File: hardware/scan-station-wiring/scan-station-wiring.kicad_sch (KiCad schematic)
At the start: 55 parts, among them J1A CYD Expansion (SPI2), J1B CYD UART (PWR+HS), J2 NFC Antenna A, J3 RGB LED Header, J4 NFC Antenna B, J5 USB-C Power, J6 Load Cell, J7 CAN Bus, J8 I2C1 Expansion, J9 TOF Sensor (I2C1), Q1 TVDD_SW_A, Q2 TVDD_SW_B, Q3 BSS138 (SDA), Q4 BSS138 (SCL), U1 ESP32-S3-DevKitC-1, U2 ADS1220IPWR, U3 AHT20, U4 PN5180A0HN, U5 AS7341-DLGM, U6 AMS1117-3.3, U7 SN65HVD230DR, U8 AMS1117-1.8, Y1 27.12MHz

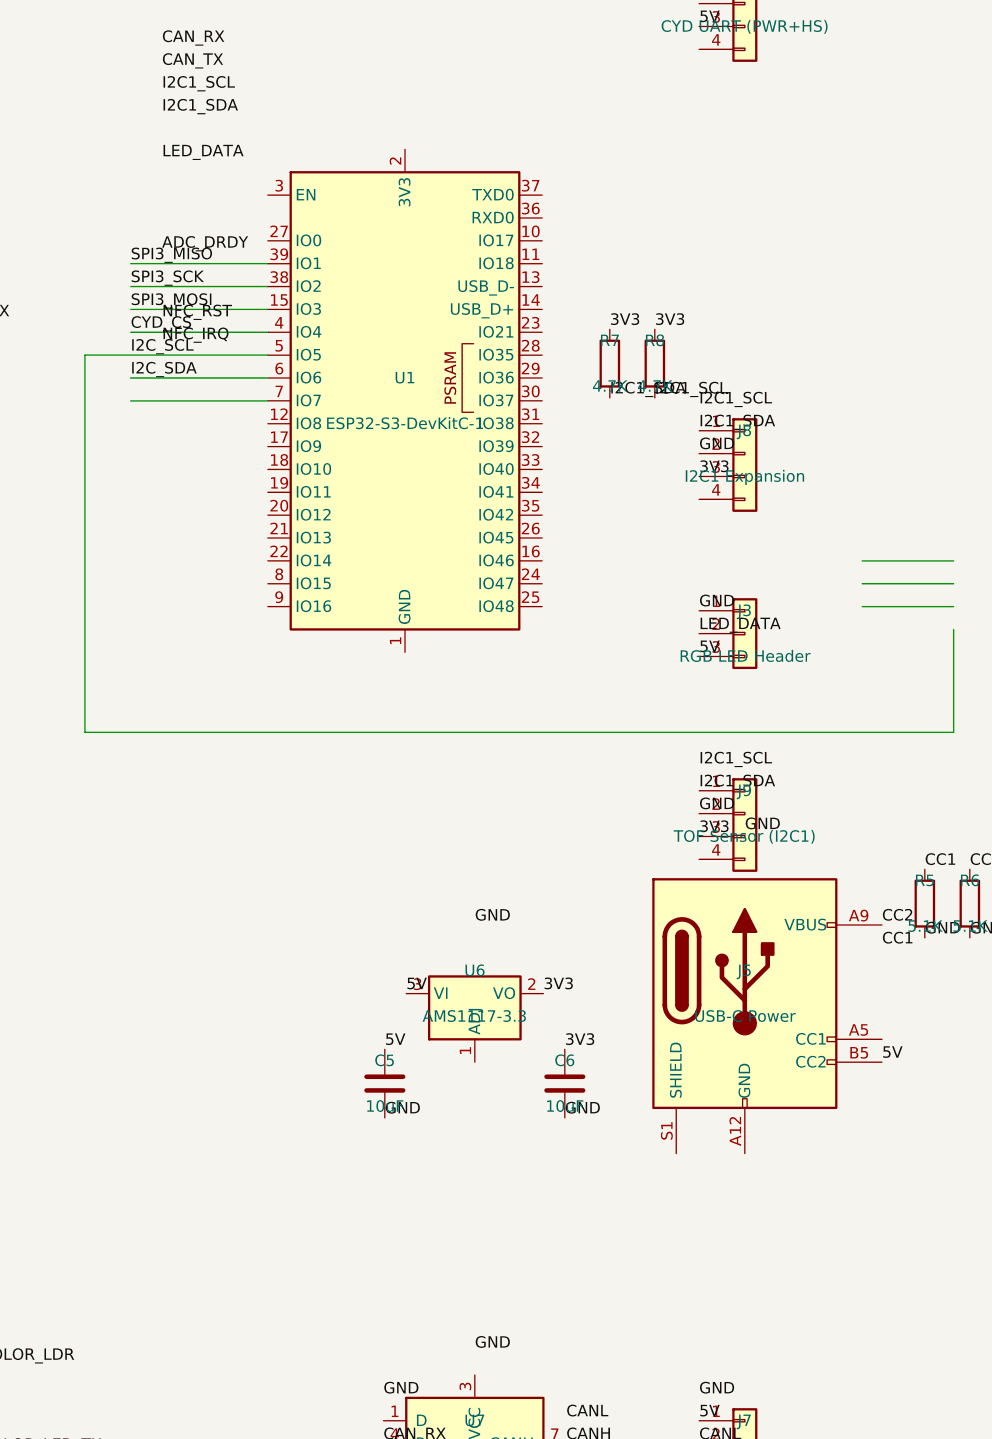
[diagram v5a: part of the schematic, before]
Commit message: feat: add button/encoder header for non-touchscreen operation
J10: 5-pin header for rotary encoder (A/B/SW) or 3 buttons
- BTN_A (IO35), BTN_B (IO36), BTN_SW (IO37) + 3V3 + GND
- Enables non-CYD configurations (SPI OLED + physical controls)
- CYD_SPARE/CYD_READY pins double as DC/RST for dumb SPI displays

Co-Authored-By: Claude Opus 4.6 (1M context) <noreply@anthropic.com>
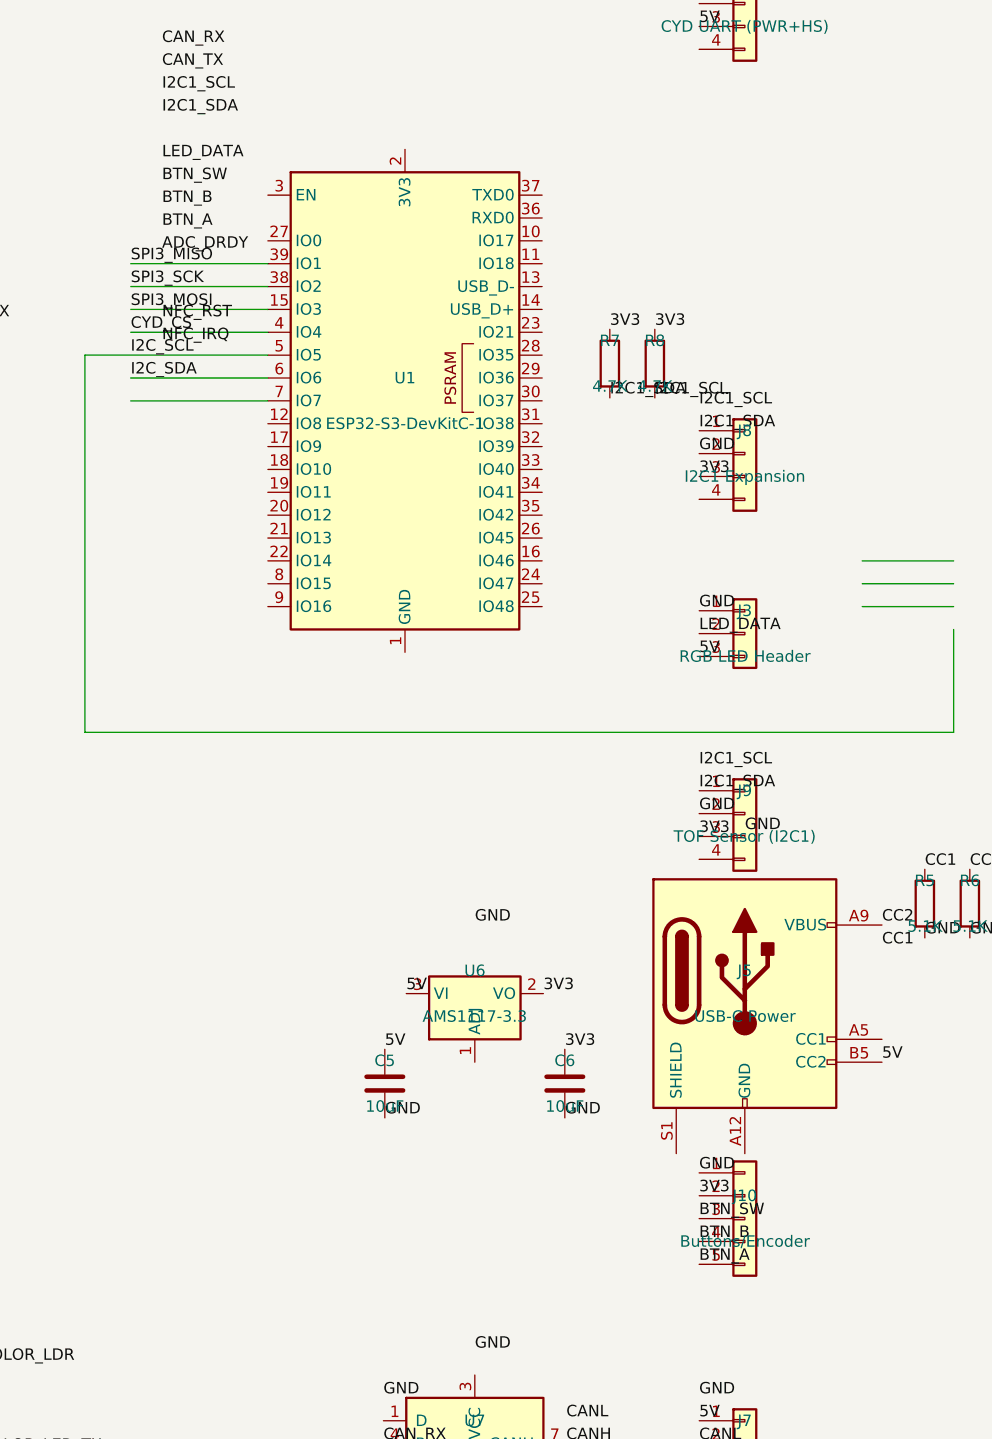
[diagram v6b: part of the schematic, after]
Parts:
- added J10: Buttons/Encoder, symbol Connector_Generic:Conn_01x05
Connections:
- net 3V3: now also J10.2 (Pin_2)
- net GND: now also J10.1 (Pin_1)
- new net BTN_A: J10.5 (Pin_5)
- new net BTN_B: J10.4 (Pin_4)
- new net BTN_SW: J10.3 (Pin_3)

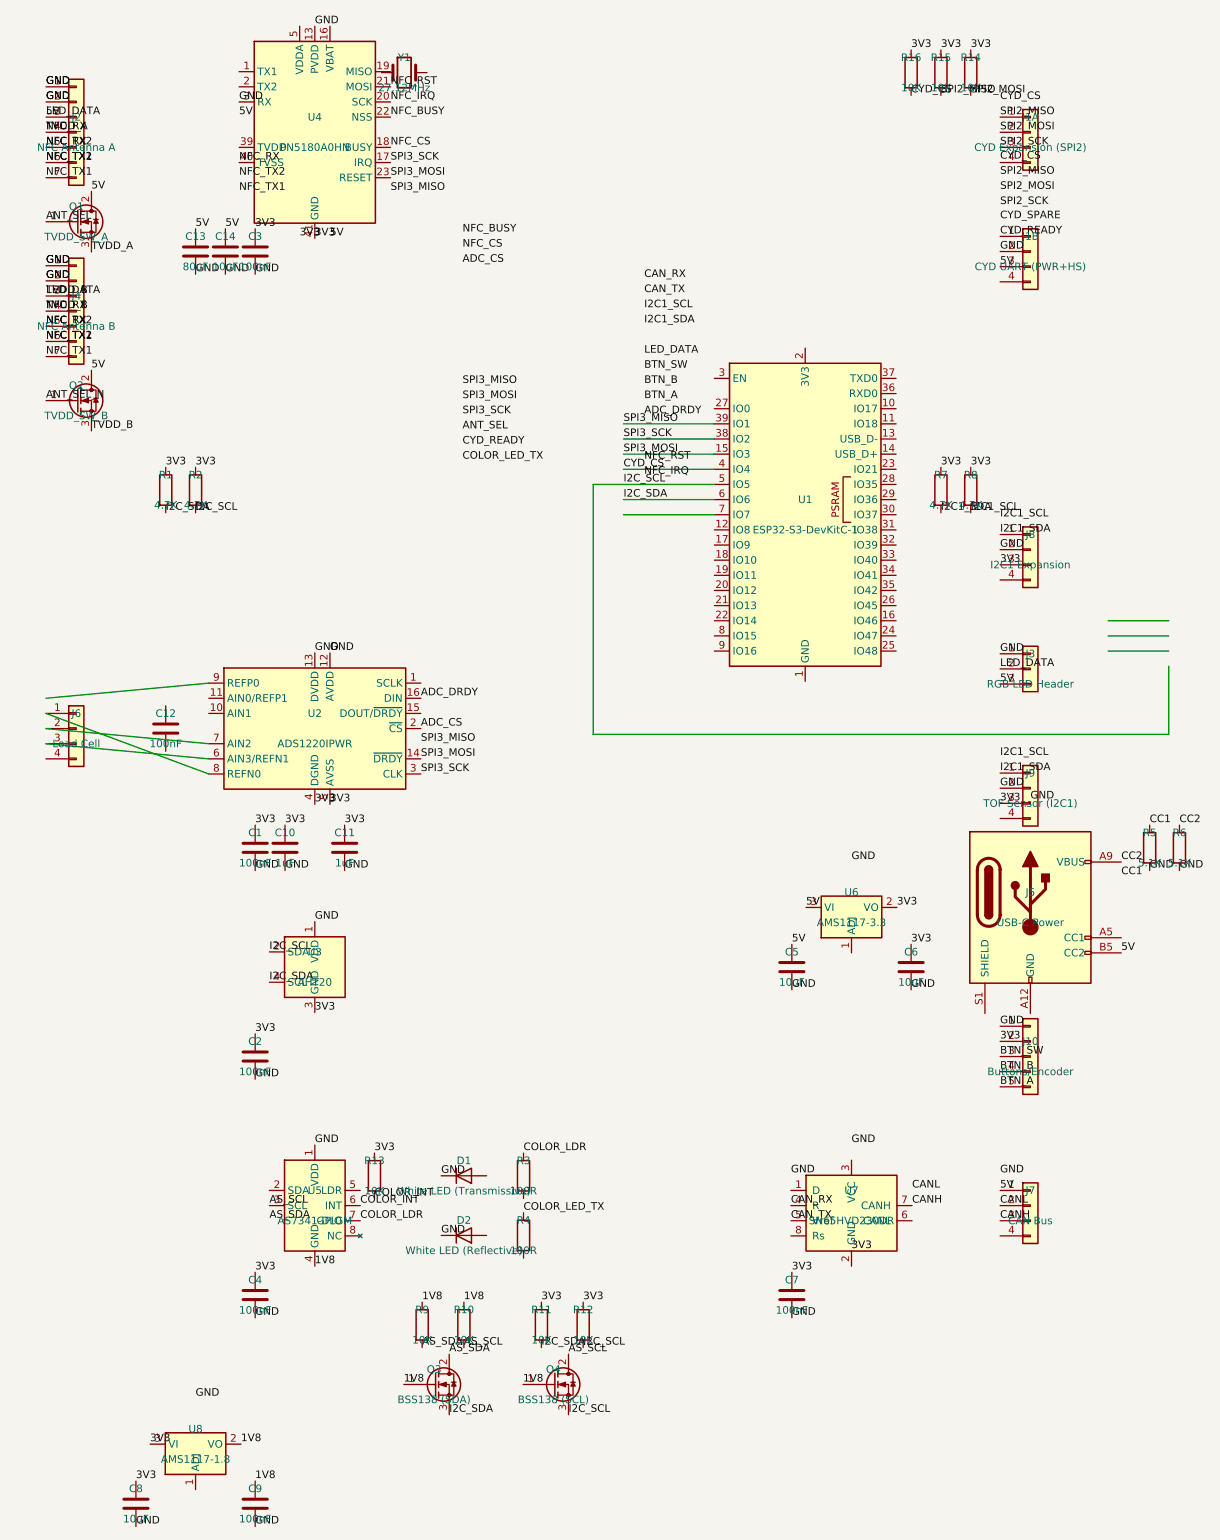
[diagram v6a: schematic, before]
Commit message: feat: add GPIO expansion header with 5 free pins
J11: 7-pin GPIO expansion header
- IO7, IO45, IO46, IO47, IO48 (5 free GPIOs)
- 3V3, GND
- All ESP32-S3 GPIOs now assigned or broken out

Co-Authored-By: Claude Opus 4.6 (1M context) <noreply@anthropic.com>
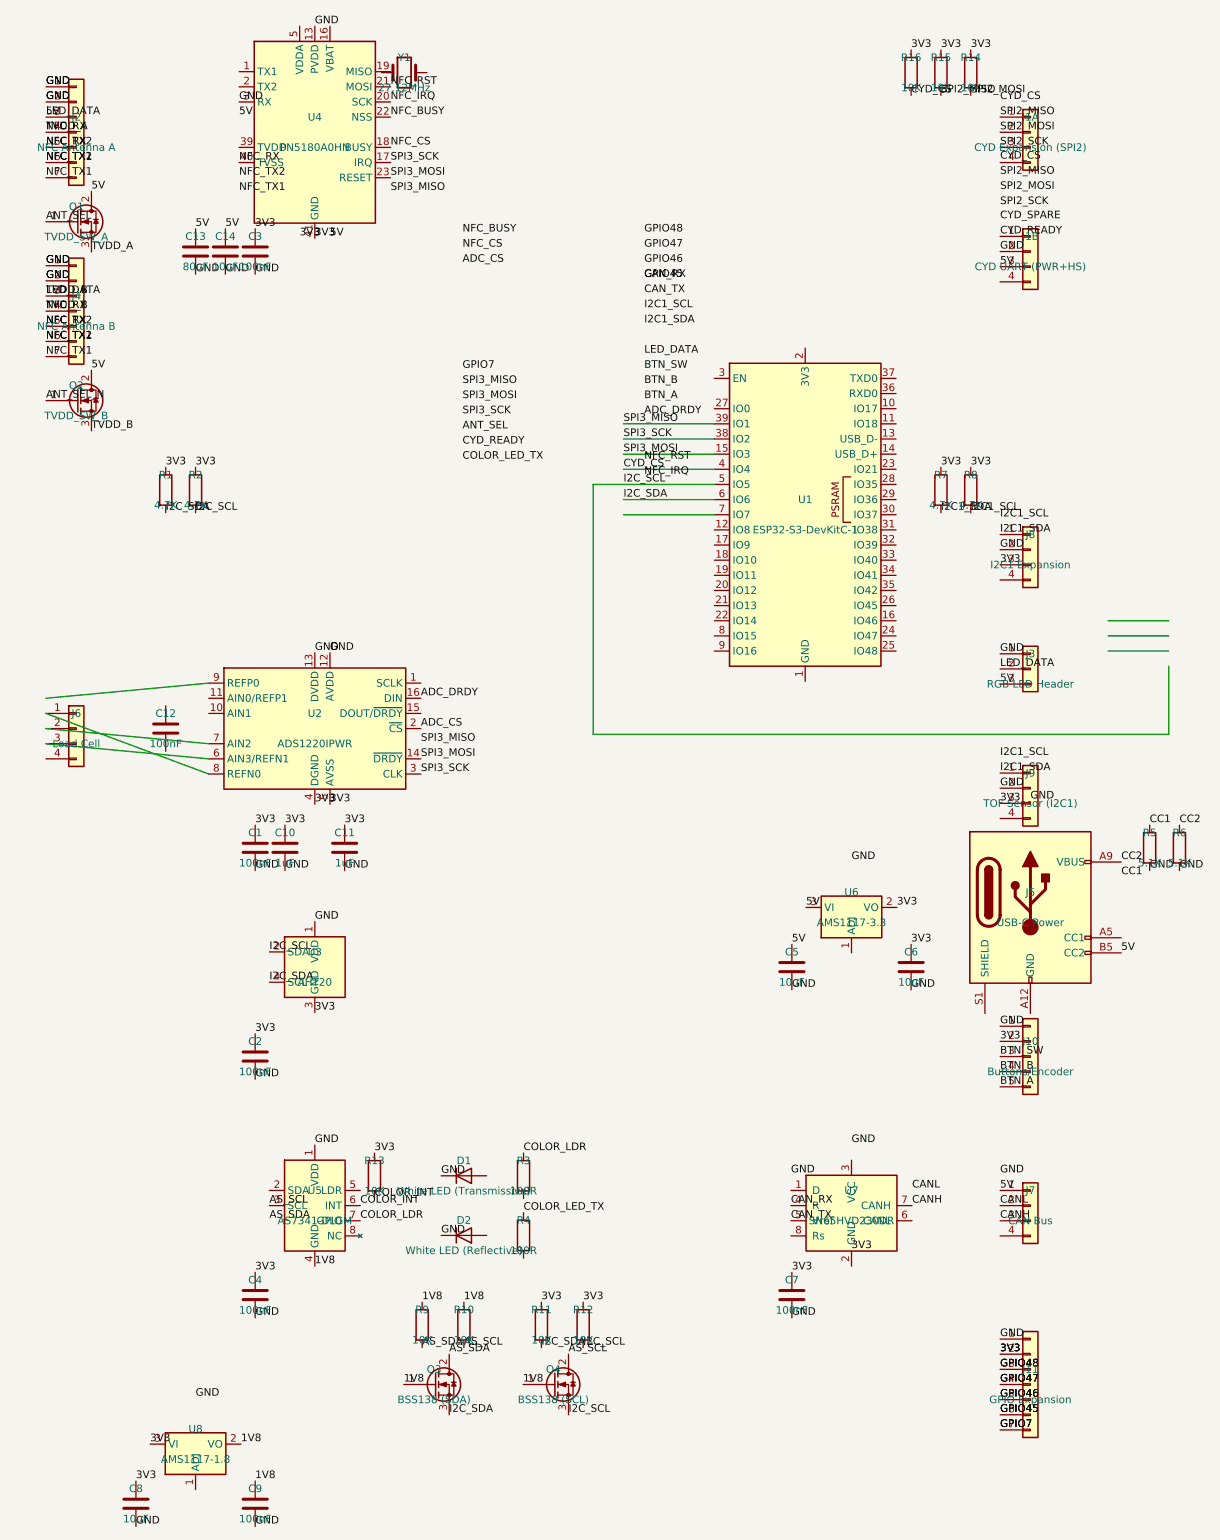
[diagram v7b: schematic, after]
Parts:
- added J11: GPIO Expansion, symbol Connector_Generic:Conn_01x07
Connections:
- net 3V3: now also J11.2 (Pin_2)
- net CAN_RX: now also J11.6 (Pin_6)
- net GND: now also J11.1 (Pin_1)
- new net GPIO46: J11.5 (Pin_5)
- new net GPIO47: J11.4 (Pin_4)
- new net GPIO48: J11.3 (Pin_3)
- new net GPIO7: J11.7 (Pin_7)
